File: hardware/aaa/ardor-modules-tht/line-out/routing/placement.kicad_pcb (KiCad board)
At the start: 2 copper layers, 115 x 85 mm, 29 parts, among them J101 5V POWER + ENABLE INPUT, J102 MONO AUDIO INPUT FROM SOURCE, J502 AUDIO OUTPUT TO AMP INPUT, J503 LINE AUDIO OUTPUT TO TS SOCKET, K501 Omron G5V-1 DC5, Q501 2N3904 / E-B-C, U501 MCP6022-I/P

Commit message: fix(hardware): use Hestore TVS diodes in hand-assembly modules
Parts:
- D501: value SA5.0CA-E3/54 -> 1.5KE6.8CA; footprint Diode_THT:D_DO-15_P10.16mm_Horizontal -> Ardor_THT:D_TVS_DC_1.5KE_P15.24mm
- moved D501 2.54 mm to (139.9, 102.5)

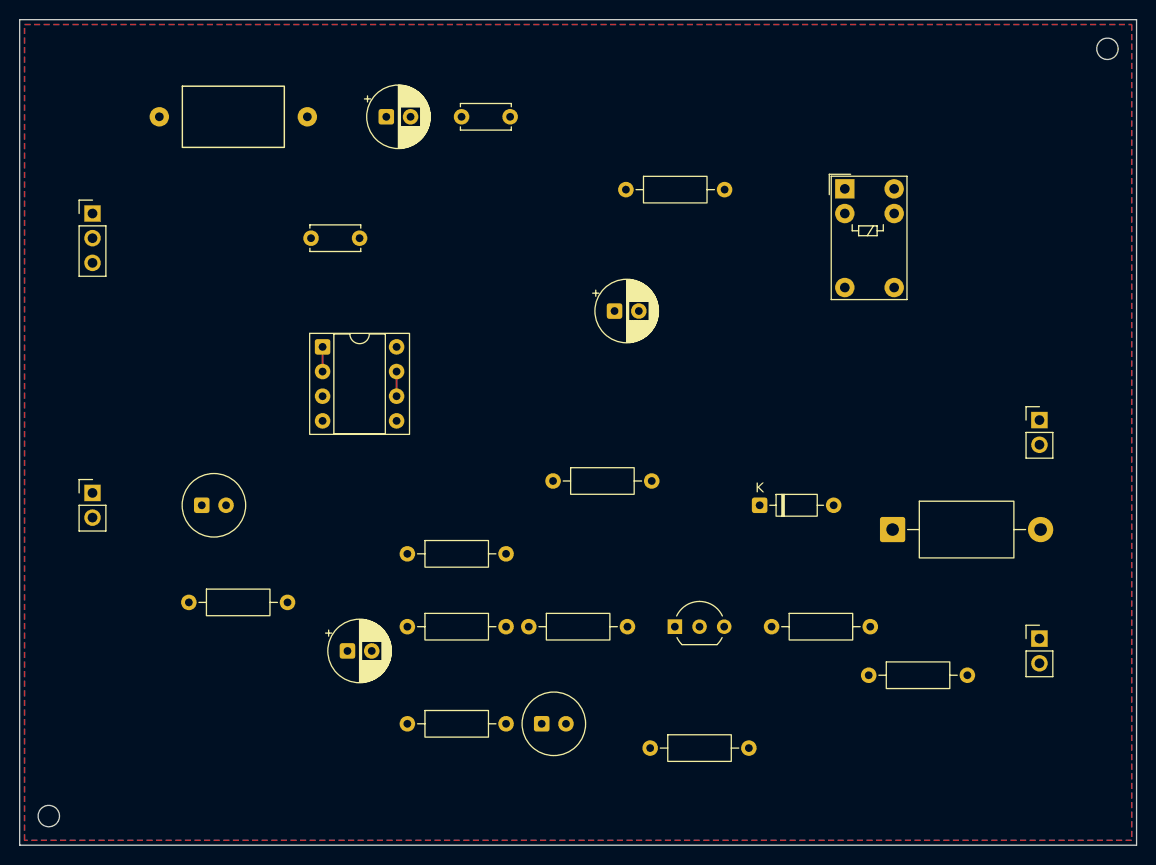
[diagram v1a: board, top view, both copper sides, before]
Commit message: feat(hardware): compact layouts and adopt Hestore module packages
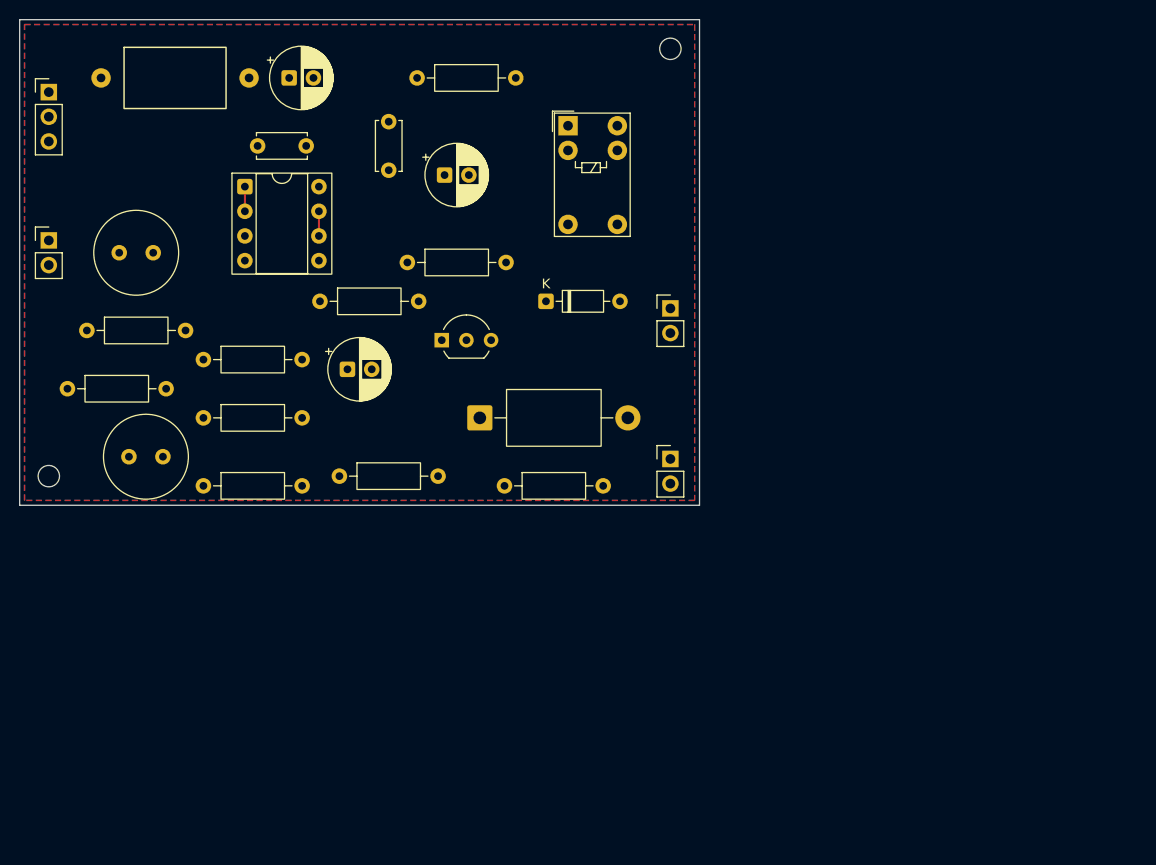
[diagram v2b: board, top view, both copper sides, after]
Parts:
- C401, C502: value 10u / 25V BIPOLAR -> 10u / 50V BIPOLAR; footprint Ardor_THT:CP_Bipolar_D6.3mm_P2.50mm -> Ardor_THT:CP_Bipolar_Nichicon_D8.0mm_P3.50mm
- moved R506 73.4 mm to (68.9, 91.0)
- moved R505 53.3 mm to (68.9, 98.0)
- moved C502 50.6 mm to (61.2, 95.0)
- moved R503 49.1 mm to (54.9, 88.0)
- moved H2 45.0 mm to (117.0, 53.0)
- moved D501 44.0 mm to (97.4, 91.0)
- moved J502 42.3 mm to (117.0, 95.2)
- moved J503 39.7 mm to (117.0, 79.7)
- moved Q501 38.0 mm to (93.5, 83.0)
- moved H1 35.0 mm to (53.0, 97.0)
- moved R406 34.7 mm to (80.9, 79.0)
- moved R101 31.1 mm to (99.9, 98.0)
- moved D502 30.4 mm to (104.2, 79.0)
- moved R401 29.9 mm to (56.9, 82.0)
- moved K501 29.2 mm to (106.5, 60.9)
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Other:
- board size 115 x 85 mm -> 70 x 50 mm
